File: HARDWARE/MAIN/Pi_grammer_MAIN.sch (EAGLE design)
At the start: 51 parts, among them J1 TARGET_copy, Q1 BSS138, Q2 BSS138, Q3 BSS138, Q4 BSS138, U1 AT42QT1010UDFN

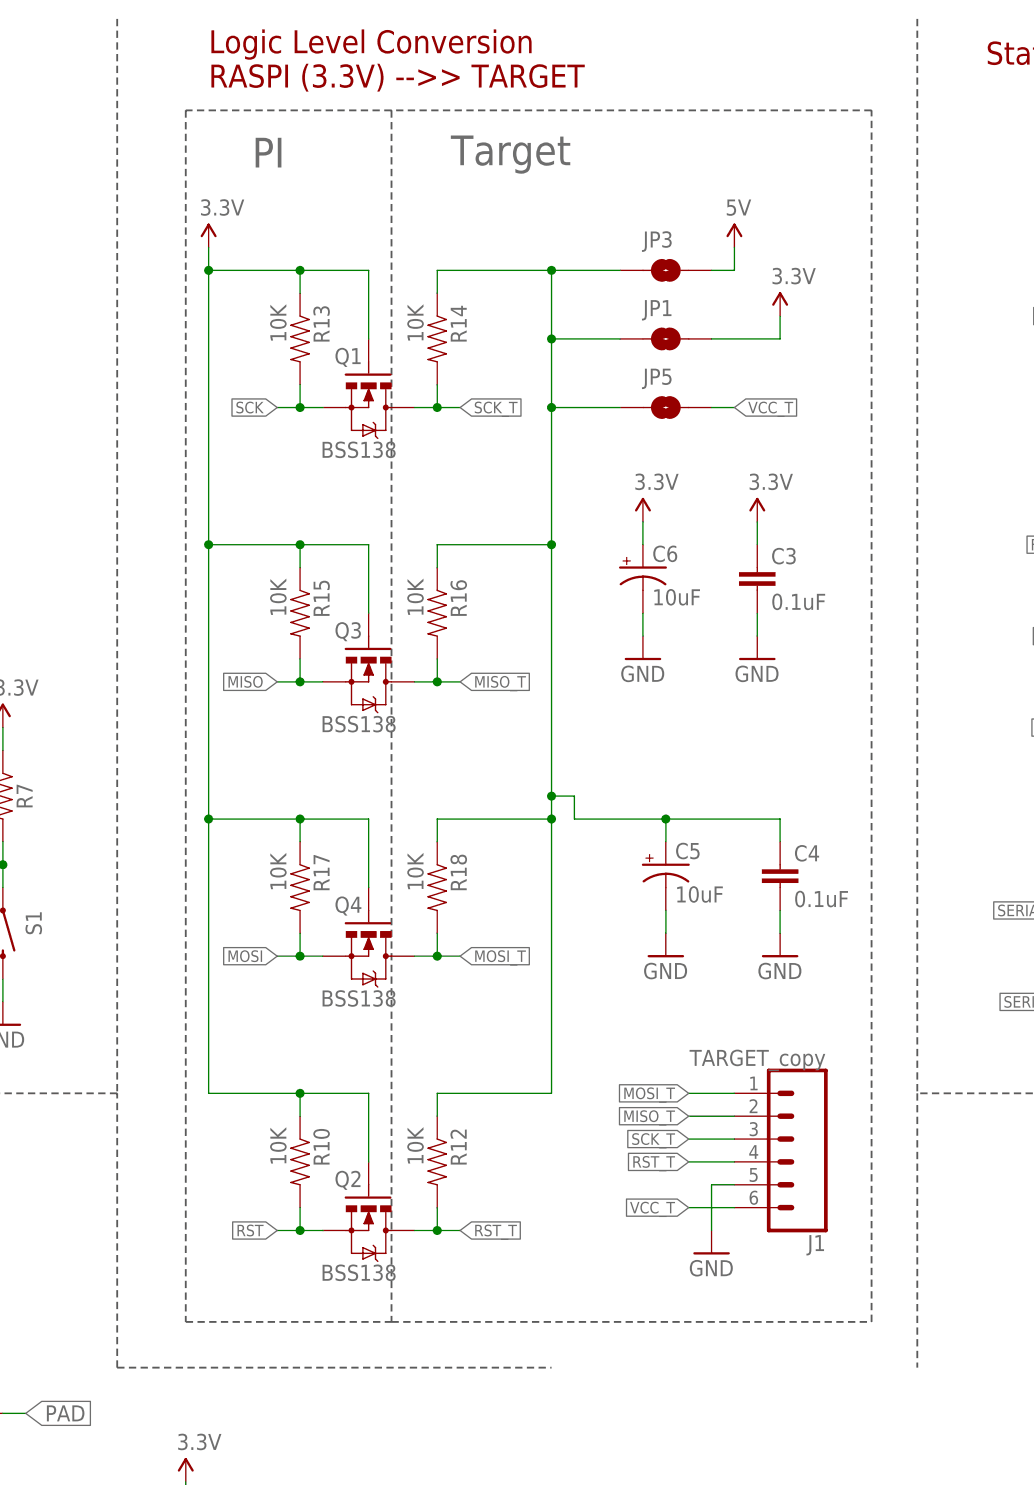
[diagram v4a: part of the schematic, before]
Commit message: BOM update - library and PROD_ID stuff
No change to design, just did a replace to correct parts in library.

Note, I also had to manually adjust the PROD_ID for the RA header,
because I didn't want to muddy up the device for this part.
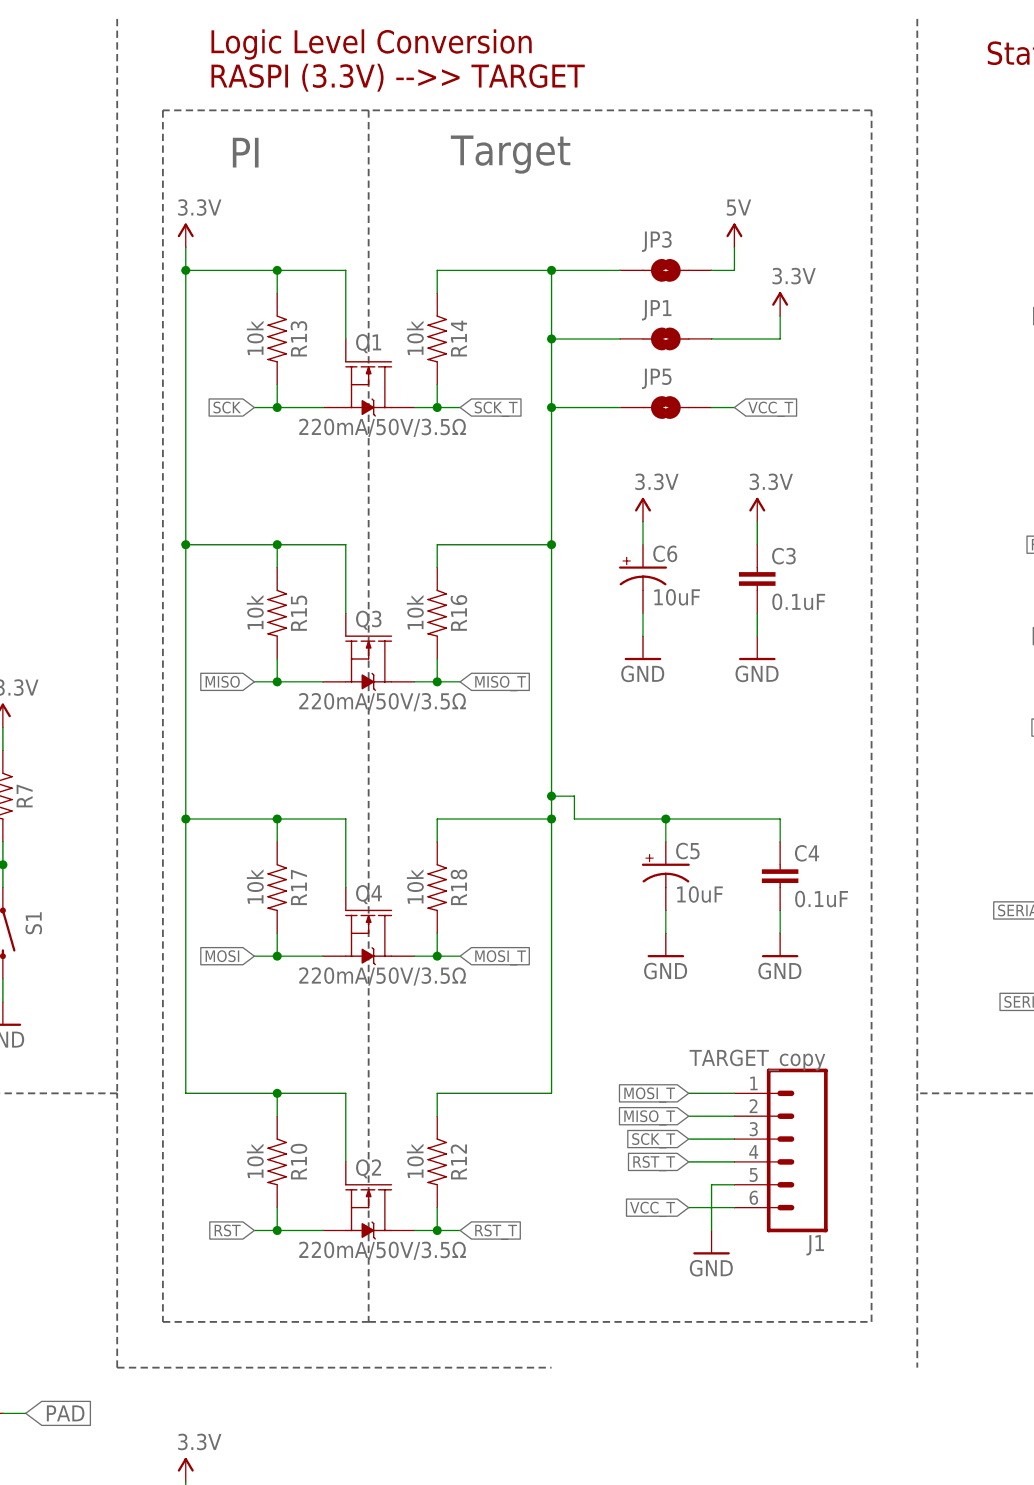
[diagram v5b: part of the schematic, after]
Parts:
- J1: device SparkFun-Connectors:CONN_06SIP_LOCK -> SparkFun-Connectors:CONN_06LOCK; PROD_ID CONN-09698 -> CONN-10140
- Q1, Q2, Q3, Q4: value BSS138 -> 220mA/50V/3.5Ω; device SparkFun:MOSFET-NCHANNELSMD -> SparkFun-DiscreteSemi:MOSFET-NCH-BSS138
- R10, R12, R13, R14, R15, R16, R17, R18: value 10K -> 10k; device SparkFun:RESISTOR0603-RES -> SparkFun-Resistors:10KOHM-0603-1/10W-1%
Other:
- moved on the sheet: R10, R13, R15, R17

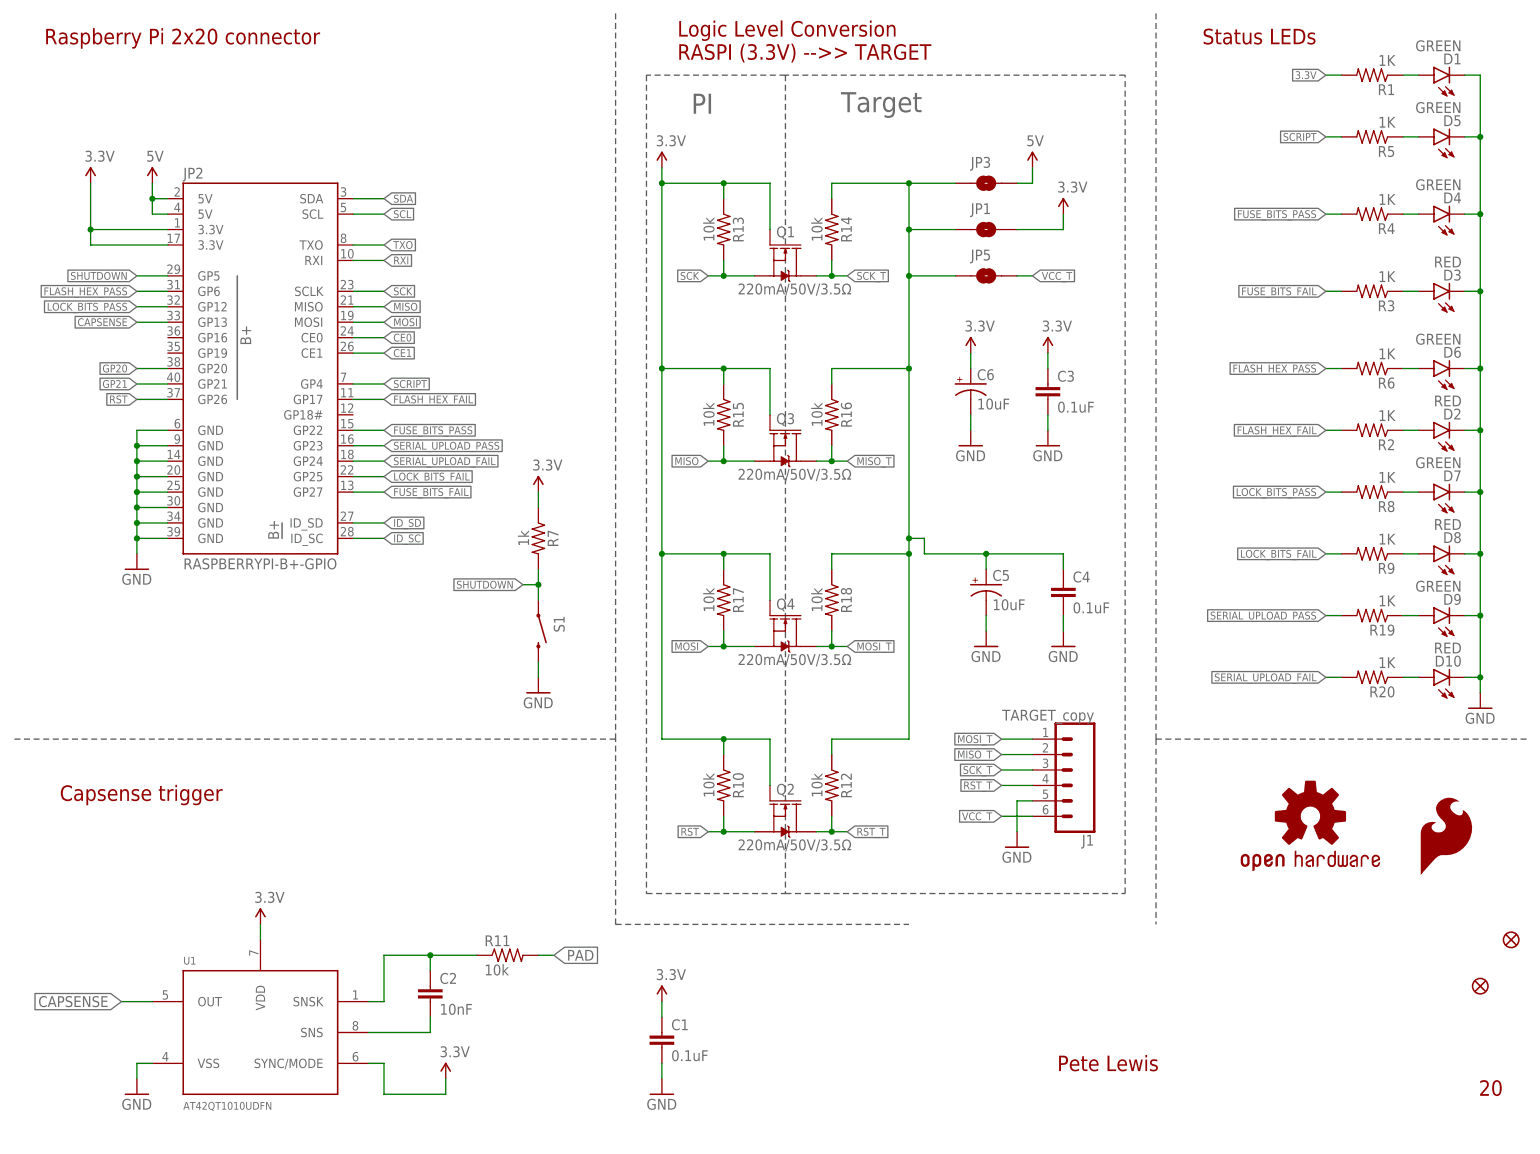
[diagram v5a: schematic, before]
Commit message: pi_grammer v21
Added in isolation switch
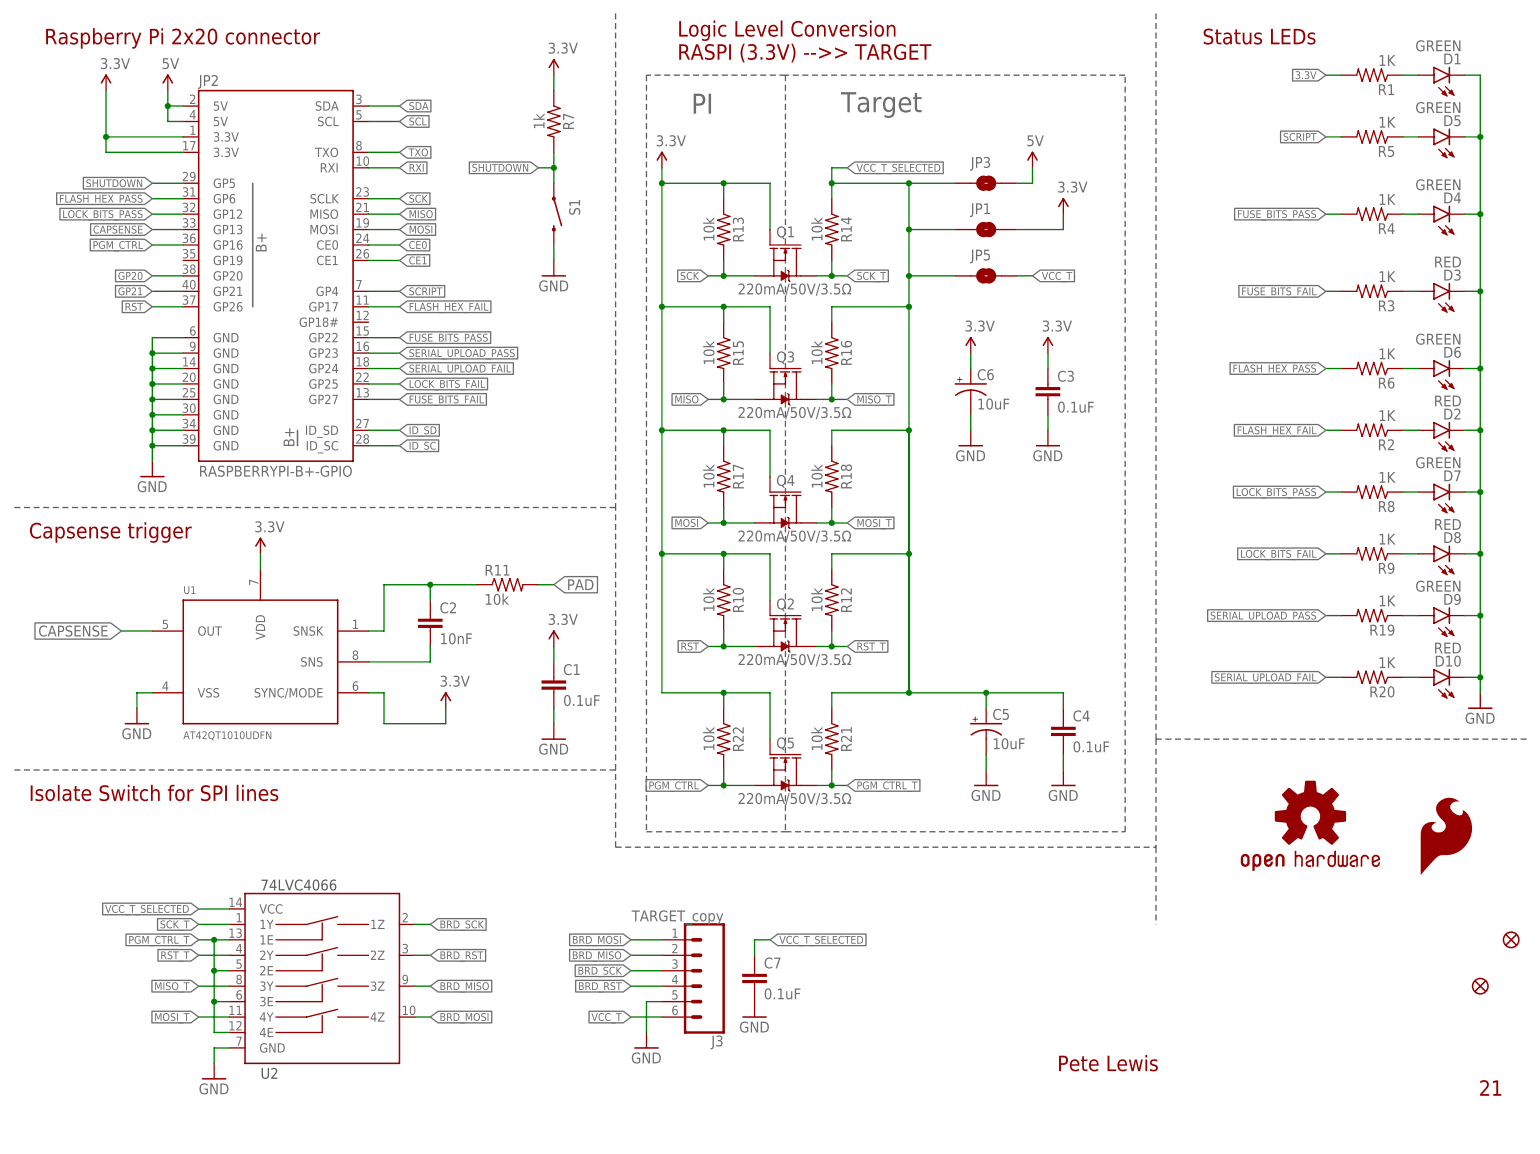
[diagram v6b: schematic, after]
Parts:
- removed J1: TARGET_copy, SparkFun-Connectors:CONN_06LOCK
- added C7: 0.1uF, SparkFun-Capacitors:0.1UF-0603-25V-(+80/-20%)
- added J3: TARGET_copy, SparkFun-Connectors:CONN_06LOCK
- added Q5: 220mA/50V/3.5Ω, SparkFun-DiscreteSemi:MOSFET-NCH-BSS138
- added R21, R22: 10k, SparkFun-Resistors:10KOHM-0603-1/10W-1%
- added U2: 74LVC4066, Testing:74LVC4066_MUX_1:1_X4
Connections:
- removed net N$9: C4.1, C5.+, JP1.1, JP3.1, JP5.1, R12.1, R14.1, R16.1, R18.1
- new net BRD_MISO: J3.2, U2.3Z
- new net BRD_MOSI: J3.1, U2.4Z
- new net BRD_RST: J3.4, U2.2Z
- new net BRD_SCK: J3.3, U2.1Z
- new net PGM_CTRL: JP2.GP16, Q5.S, R22.2
- new net PGM_CTRL_T: Q5.D, R21.2, U2.1E, U2.2E, U2.3E, U2.4E
- new net VCC_T_SELECTED: C4.1, C5.+, C7.1, JP1.1, JP3.1, JP5.1, R12.1, R14.1, R16.1, R18.1, R21.1, U2.VCC
- net 3.3V: now also Q5.G, R22.1
- net GND: now also C7.2, J3.5, U2.GND; no longer J1.5
- net MISO_T: now also U2.3Y; no longer J1.2
- net MOSI_T: now also U2.4Y; no longer J1.1
- net RST_T: now also U2.2Y; no longer J1.4
- net SCK_T: now also U2.1Y; no longer J1.3
- net VCC_T: now also J3.6; no longer J1.6
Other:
- note added: "21"
- note added: "Isolate Switch for SPI lines"
- note removed: "20"
- moved on the sheet: C1, C2, C4, C5, JP2, Q2, Q3, Q4, R10, R11, R12, R15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
